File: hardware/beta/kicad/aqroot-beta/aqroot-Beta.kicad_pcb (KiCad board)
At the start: 4 copper layers, 74 x 155 mm, 187 parts, among them J1 CH280QV10-CT_50P, J2 Molex_5025700893, J3 USB_C_Receptacle_USB2.0_16P, J4 JST-PH-2 BATTERY, J5 COMMUNITY_HEADER_2x13, J6 JST-PH-2 SPEAKER, Q1 AO3400A, SW1 BOOT, SW2 UP, SW3 DOWN, SW4 LEFT, SW5 RIGHT, SW6 A_SELECT, SW7 B_BACK, SW8 HOME, SW9 SW_SPDT, U1 ESP32-S3-WROOM-1, U10 USBLC6-2SC6, U11 BQ25185, U12 TPS63020, U13 TPS61023, U14 MAX17048, U15 TPS22918, U16 TCA9517ADGK, U17 TPS61169DCKR, U2 TCA9535PWR, U3 TCA9535PWR, U4 BMI270, U5 MAX98357A, U6 TSOP38238, U7 E07-400M10S, U8 E22-900M22S, U9 ST25R3916-AQET

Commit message: AQROOT Beta: close final routing blockers
Closes the two BLOCKS_ROUTING items left by the pre-routing rule pass.
No traces drawn, no component moved, aqroot-Beta.kicad_dru untouched.

1. BQ25185 charge current locked at 300 mA.

R37 2k 1% -> 1k 1% on the ISET pin. ICHG = KISET/RISET = 300/1000 =
300 mA typ, 285/300/315 mA from the KISET spread and 270-330 mA at
TI's +/-10% ICHG_ACC spec. 0.15 C on the 2000 mAh Beta pack. IPRECHG
rises to 60 mA and ITERM to 30 mA. 1 kohm is TI's own figure in
SLUSF65A section 8.2.2.2, is far above RISET_SHORT (264 ohm), and
300 mA is far below the 1 A device maximum, so nothing is clipped.

R36 = 18 kohm is untouched: the input current limit stays ILIM500
(450/475/498 mA) and VBATREG stays 4.2 V. Both the schematic symbol and
the PCB footprint Value field were updated together, so parity picks up
no new field mismatch.

No power netclass width target changes. VBUS_CHG is set by ILIM, which
did not move; BAT_MAIN is sized by 1.5 A discharge and 3.125 A OCP;
SYS_MAIN is sized by the ~750 mA system load. IPC-2221B needs 0.057 mm
for 300 mA on 1 oz outer copper at dT=10 K, an order of magnitude below
every existing floor, so nothing was widened.

The real consequence is thermal and lands on U11. As a linear charger
with a power path, worst-case dissipation rises from ~0.46 W to ~0.69 W
(0.238 W on IN->SYS at 475 mA plus 0.450 W on the BATFET at 300 mA into
a depleted 3.0 V pack) in a 2.2 x 2.0 mm WSON-10. TREG folds charge
current back rather than failing, so this is a charge-time risk, but
U11's exposed-pad thermal vias are now required rather than optional
and the plan is revised from 1 to 2 THERMAL-class vias. Implementation
stays deferred to the routing/thermal pass.

Added BOM VERIFY: the cell/pack must permit >=300 mA charge, including
the pack protection circuit's own rating. Blocks BOM lock, not routing.

2. USB differential net names normalised to a _P/_N suffix.

  USB_D_P_CONN -> USB_D_CONN_P    USB_D_N_CONN -> USB_D_CONN_N
  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
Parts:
- R37: value 2k 1% -> 1k 1%
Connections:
- net /01_POWER_TREE/USB_D_N_CONN renamed /01_POWER_TREE/USB_D_CONN_N
- net /01_POWER_TREE/USB_D_N_ESD renamed /01_POWER_TREE/USB_D_ESD_N
- net /01_POWER_TREE/USB_D_P_CONN renamed /01_POWER_TREE/USB_D_CONN_P
- net /01_POWER_TREE/USB_D_P_ESD renamed /01_POWER_TREE/USB_D_ESD_P
- net /USB_D_N_MCU renamed /USB_D_MCU_N
- net /USB_D_P_MCU renamed /USB_D_MCU_P
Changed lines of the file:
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@@
 			(layers "F.Cu" "F.Mask" "F.Paste")
 			(roundrect_rratio 0.25)
-			(net "/01_POWER_TREE/USB_D_N_ESD")
+			(net "/01_POWER_TREE/USB_D_ESD_N")
 		)
 		(pad "2" smd roundrect
@@
 			(layers "F.Cu" "F.Mask" "F.Paste")
 			(roundrect_rratio 0.25)
-			(net "/USB_D_N_MCU")
+			(net "/USB_D_MCU_N")
 		)
 		(embedded_fonts no)
@@
 			(layers "F.Cu" "F.Mask" "F.Paste")
 			(roundrect_rratio 0.25)
-			(net "/USB_D_N_MCU")
+			(net "/USB_D_MCU_N")
 		)
 		(pad "2" smd roundrect
@@
 			(layers "F.Cu" "F.Mask" "F.Paste")
 			(roundrect_rratio 0.25)
-			(net "/USB_D_P_MCU")
+			(net "/USB_D_MCU_P")
 		)
 		(pad "2" smd roundrect
@@
 			(layers "F.Cu" "F.Mask" "F.Paste")
 			(roundrect_rratio 0.25)
-			(net "/01_POWER_TREE/USB_D_P_ESD")
+			(net "/01_POWER_TREE/USB_D_ESD_P")
 		)
 		(pad "2" smd roundrect
@@
 			(layers "F.Cu" "F.Mask" "F.Paste")
 			(roundrect_rratio 0.25)
-			(net "/USB_D_P_MCU")
+			(net "/USB_D_MCU_P")
 		)
 		(embedded_fonts no)
@@
 			)
 		)
-		(property "Value" "2k 1%"
+		(property "Value" "1k 1%"
 			(at 0 1.43 0)
 			(layer "F.Fab")
@@
 			(layers "F.Cu" "F.Mask" "F.Paste")
 			(roundrect_rratio 0.25)
-			(net "/01_POWER_TREE/USB_D_N_CONN")
+			(net "/01_POWER_TREE/USB_D_CONN_N")
 		)
 		(pad "2" smd roundrect
@@
 			(layers "F.Cu" "F.Mask" "F.Paste")
 			(roundrect_rratio 0.25)
-			(net "/01_POWER_TREE/USB_D_P_CONN")
+			(net "/01_POWER_TREE/USB_D_CONN_P")
 		)
 		(pad "4" smd roundrect
@@
 			(layers "F.Cu" "F.Mask" "F.Paste")
 			(roundrect_rratio 0.25)
-			(net "/01_POWER_TREE/USB_D_P_ESD")
+			(net "/01_POWER_TREE/USB_D_ESD_P")
 		)
 		(pad "5" smd roundrect
@@
 			(layers "F.Cu" "F.Mask" "F.Paste")
 			(roundrect_rratio 0.25)
-			(net "/01_POWER_TREE/USB_D_N_ESD")
+			(net "/01_POWER_TREE/USB_D_ESD_N")
 		)
 		(embedded_fonts no)
@@
 			(layers "F.Cu" "F.Mask" "F.Paste")
 			(roundrect_rratio 0.25)
-			(net "/01_POWER_TREE/USB_D_P_CONN")
+			(net "/01_POWER_TREE/USB_D_CONN_P")
 		)
 		(pad "A7" smd roundrect
@@
 			(layers "F.Cu" "F.Mask" "F.Paste")
 			(roundrect_rratio 0.25)
-			(net "/01_POWER_TREE/USB_D_N_CONN")
+			(net "/01_POWER_TREE/USB_D_CONN_N")
 		)
 		(pad "A8" smd roundrect
@@
 			(layers "F.Cu" "F.Mask" "F.Paste")
 			(roundrect_rratio 0.25)
-			(net "/01_POWER_TREE/USB_D_P_CONN")
+			(net "/01_POWER_TREE/USB_D_CONN_P")
 		)
 		(pad "B7" smd roundrect
@@
 			(layers "F.Cu" "F.Mask" "F.Paste")
 			(roundrect_rratio 0.25)
-			(net "/01_POWER_TREE/USB_D_N_CONN")
+			(net "/01_POWER_TREE/USB_D_CONN_N")
 		)
 		(pad "B8" smd roundrect
@@
 			(size 1.5 0.9)
 			(layers "B.Cu" "B.Mask" "B.Paste")
-			(net "/USB_D_N_MCU")
+			(net "/USB_D_MCU_N")
 		)
 		(pad "14" smd rect
@@
 			(size 1.5 0.9)
 			(layers "B.Cu" "B.Mask" "B.Paste")
-			(net "/USB_D_P_MCU")
+			(net "/USB_D_MCU_P")
 		)
 		(pad "15" smd rect

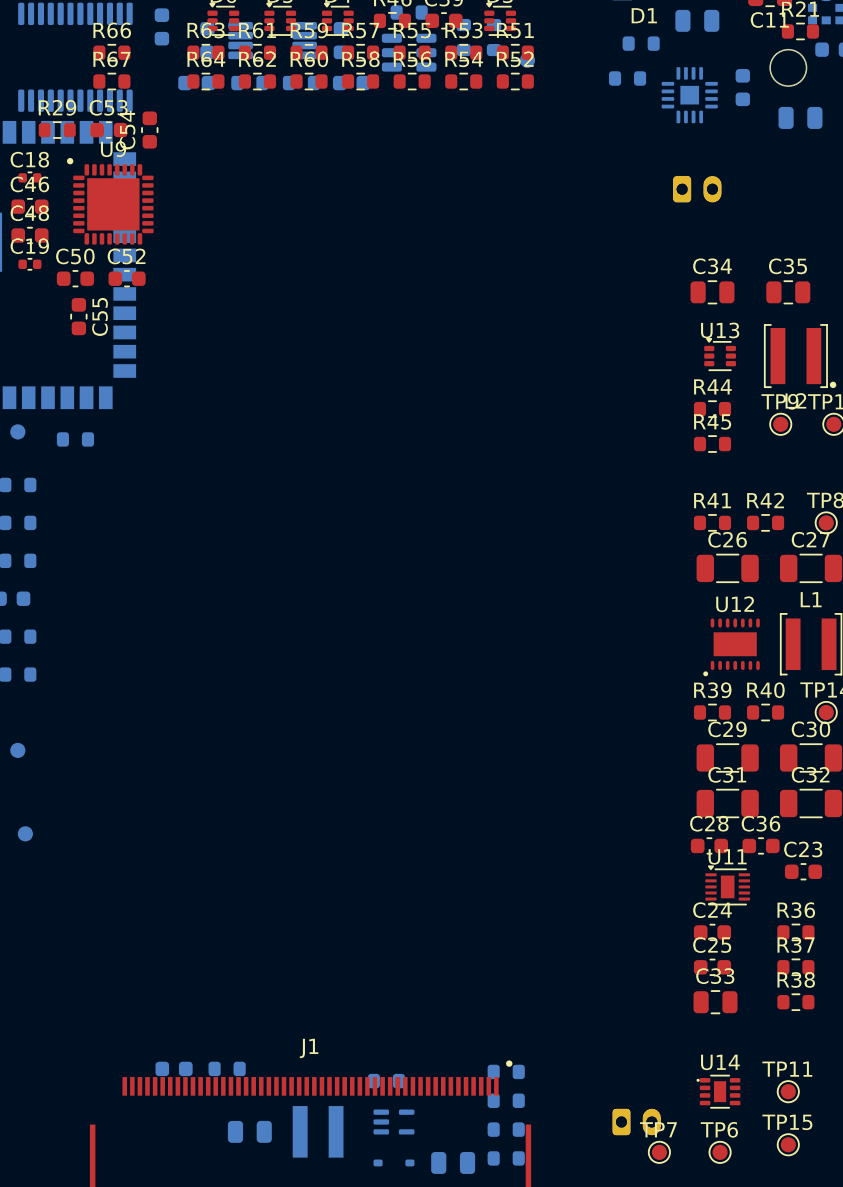
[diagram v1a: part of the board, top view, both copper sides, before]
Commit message: AQROOT Beta: route GND reference and exposed-pad thermal infrastructure
Routing Pass 1, PARTIAL. Blocks A and B of the pass scope are routed and
DRC-clean. Blocks C-F (converters, major power rails, USB, E4/E5
crossings, critical decoupling loops) were routed, produced 41 DRC
errors, and were REVERTED rather than committed. Nothing broken is in
this commit. Placement, connectivity and ERC are untouched, and no
signal trace exists on the board - GND is the only net carrying copper.

Delivered:

In1 GND reference zone, one pour inset 0.6 mm from the board edge:
10025.8 mm2 filled of an 11181.0 mm2 outline. The 1155 mm2 shortfall is
three pre-existing all-layer rule areas plus pad clearance. Two are
electrically required (WROOM antenna, NFC loop). HEADER RESERVED is a
37 x 8.5 mm hole in the reference plane with no manufacturer requirement
behind it - left in place, flagged for the CTO.

16 exposed-pad thermal vias at the THERMAL class (0.25/0.55), each array
the maximum its vendor land pattern accepts with >=0.10 mm margin. TI
SLUSF65A 8.4.1 asks for "a solid ground plane tied to the GND pin and
thermal pad" and specifies no via count, so none was invented. U11 2,
U12 6, U9 6, U5 1, U14 1. U1 needed nothing: the WROOM footprint already
carries 12 integral plated 0.20 mm vias in pad 41.

U9's exposed pad sits on top of the WROOM pad column: U1's B.Cu pads
15-30 occupy X 24.500-26.000 directly beneath the eastern half of U9's
EP land, so a through via there would short the NFC reader's ground to a
WROOM GPIO. Only the western strip is usable - 6 vias instead of 9, all
offset to one side. Placement-stack consequence, carried as an RF and
thermal review item.

KiCad custom-rule precedence is LAST-match-wins, established empirically
twice in this pass because the first assumption was wrong. aqroot-Beta
.kicad_dru now ends with an explicit PRECEDENCE TAIL documenting the
required weakest-first order: RF and rail rules, then pad-escape
necking, then land-pattern rules. Movin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
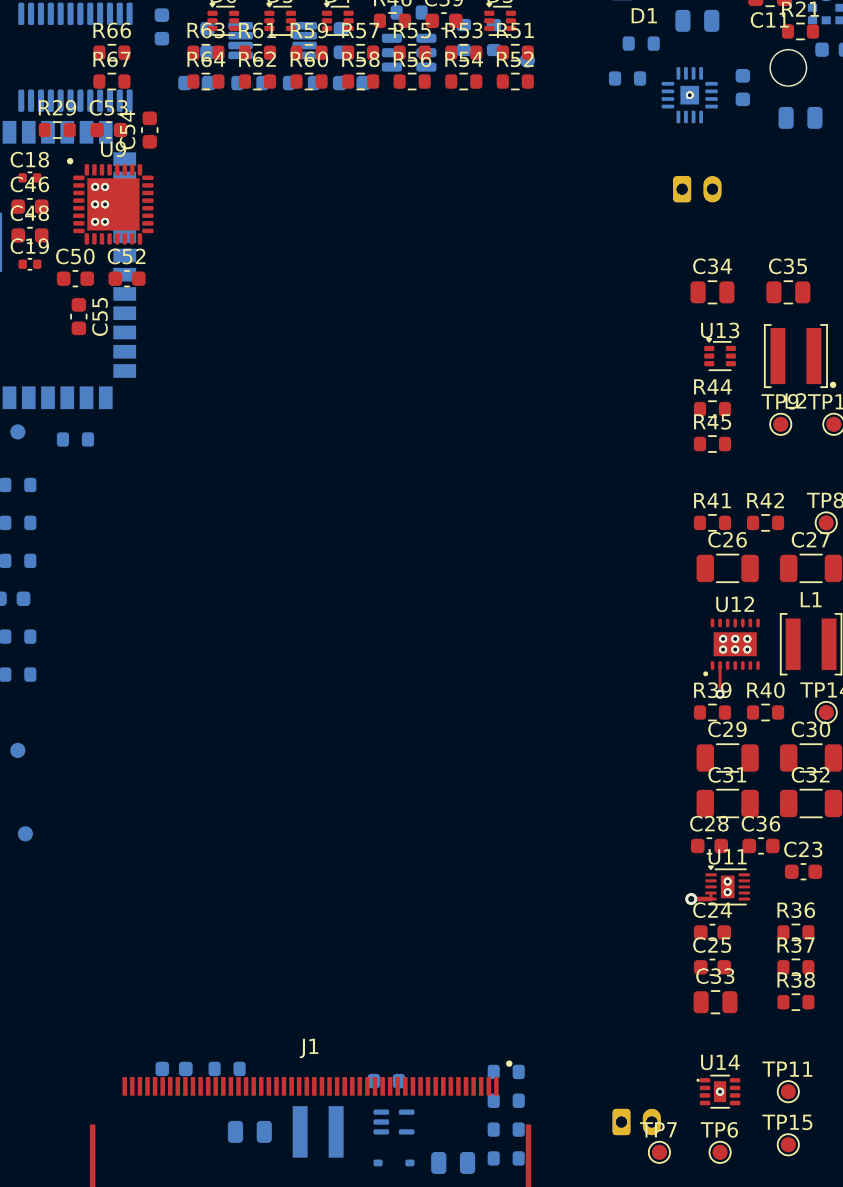
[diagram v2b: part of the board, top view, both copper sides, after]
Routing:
- net GND: track 0.00 -> 3.20 mm, vias 0 -> 18
- added copper zone on In1.Cu, net GND
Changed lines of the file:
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@@
 	(footprint "C_0603_1608Metric"
 		(layer "F.Cu")
-		(at 22 26.9)
+		(at 22.225 29.4 -90)
 		(descr "Capacitor SMD 0603 (1608 Metric), square (rectangular) end terminal, IPC-7351 nominal, (Body size source: IPC-SM-782 page 76, https://www.pcb-3d.com/wordpress/wp-content/uploads/ipc-sm-782a_amendment_1_and_2.pdf)")
 		(tags "capacitor")
-		(property "Reference" "C50"
-			(at 0 -1.43 0)
+		(property "Reference" "C55"
+			(at 0 -1.43 270)
 			(layer "F.SilkS")
 			(effects
@@
 			)
 		)
-		(property "Value" "10nF"
-			(at 0 1.43 0)
+		(property "Value" "2.2uF"
+			(at 0 1.43 270)
 			(layer "F.Fab")
 			(effects
@@
 		)
 		(property "Datasheet" ""
-			(at 0 0 0)
+			(at 0 0 270)
 			(layer "F.Fab")
 			(hide yes)
@@
 		)
 		(property "Description" ""
-			(at 0 0 0)
+			(at 0 0 270)
 			(layer "F.Fab")
 			(hide yes)
@@
 		)
 		(property "KiLib_Generator" "SMD_2terminal_chip_molded"
-			(at 0 0 0)
+			(at 0 0 270)
 			(layer "F.SilkS")
 			(hide yes)
@@
 		(duplicate_pad_numbers_are_jumpers no)
 		(fp_line
-			(start -0.14058 -0.51)
-			(end 0.14058 -0.51)
+			(start -0.14058 0.51)
+			(end 0.14058 0.51)
 			(stroke
 				(width 0.12)
@@
 		)
 		(fp_line
-			(start -0.14058 0.51)
-			(end 0.14058 0.51)
+			(start -0.14058 -0.51)
+			(end 0.14058 -0.51)
 			(stroke
 				(width 0.12)
@@
 		)
 		(fp_text user "${REFERENCE}"
-			(at 0 0 0)
+			(at 0 0 270)
 			(layer "F.Fab")
 			(effects
@@
 		)
 		(pad "1" smd roundrect
-			(at -0.775 0)
+			(at -0.775 0 270)
 			(size 0.9 0.95)
 			(layers "F.Cu" "F.Mask" "F.Paste")
 			(roundrect_rratio 0.25)
-			(net "/04_SPI_B_RADIOS_NFC/NFC_VDD_RF")
+			(net "/NFC_5V_PA_PENDING")
 		)
 		(pad "2" smd roundrect
-			(at 0.775 0)
+			(at 0.775 0 270)
 			(size 0.9 0.95)
 			(layers "F.Cu" "F.Mask" "F.Paste")
@@
 	(footprint "C_0603_1608Metric"
 		(layer "F.Cu")
-		(at 22.225 29.4 -90)
+		(at 22 26.9)
 		(descr "Capacitor SMD 0603 (1608 Metric), square (rectangular) end terminal, IPC-7351 nominal, (Body size source: IPC-SM-782 page 76, https://www.pcb-3d.com/wordpress/wp-content/uploads/ipc-sm-782a_amendment_1_and_2.pdf)")
 		(tags "capacitor")
-		(property "Reference" "C55"
-			(at 0 -1.43 270)
+		(property "Reference" "C50"
+			(at 0 -1.43 0)
 			(layer "F.SilkS")
 			(effects
@@
 			)
 		)
-		(property "Value" "2.2uF"
-			(at 0 1.43 270)
+		(property "Value" "10nF"
+			(at 0 1.43 0)
 			(layer "F.Fab")
 			(effects
@@
 		)
 		(property "Datasheet" ""
-			(at 0 0 270)
+			(at 0 0 0)
 			(layer "F.Fab")
 			(hide yes)
@@
 		)
 		(property "Description" ""
-			(at 0 0 270)
+			(at 0 0 0)
 			(layer "F.Fab")
 			(hide yes)
@@
 		)
 		(property "KiLib_Generator" "SMD_2terminal_chip_molded"
-			(at 0 0 270)
+			(at 0 0 0)
 			(layer "F.SilkS")
 			(hide yes)
@@
 		(duplicate_pad_numbers_are_jumpers no)
 		(fp_line
-			(start -0.14058 0.51)
-			(end 0.14058 0.51)
+			(start -0.14058 -0.51)
+			(end 0.14058 -0.51)
 			(stroke
 				(width 0.12)
@@
 		)
 		(fp_line
-			(start -0.14058 -0.51)
-			(end 0.14058 -0.51)
+			(start -0.14058 0.51)
+			(end 0.14058 0.51)
 			(stroke
 				(width 0.12)
@@
 		)
 		(fp_text user "${REFERENCE}"
-			(at 0 0 270)
+			(at 0 0 0)
 			(layer "F.Fab")
 			(effects
@@
 		)
 		(pad "1" smd roundrect
-			(at -0.775 0 270)
+			(at -0.775 0)
 			(size 0.9 0.95)
 			(layers "F.Cu" "F.Mask" "F.Paste")
 			(roundrect_rratio 0.25)
-			(net "/NFC_5V_PA_PENDING")
+			(net "/04_SPI_B_RADIOS_NFC/NFC_VDD_RF")
 		)
 		(pad "2" smd roundrect
-			(at 0.775 0 270)
+			(at 0.775 0)
 			(size 0.9 0.95)
 			(layers "F.Cu" "F.Mask" "F.Paste")
@@
 		)
 	)
+	(segment
+		(start 63.9 67.4)
+		(end 63.9 67.8)
+		(width 0.2)
+		(layer "F.Cu")
+		(net "GND")
+	)
+	(segment
+		(start 64.5 52.4)
+		(end 64.5 53.9)
+		(width 0.2)
+		(layer "F.Cu")
+		(net "GND")
+	)
+	(segment
+		(start 63.9 67.8)
+		(end 62.6 67.8)
+		(width 0.3)
+		(layer "F.Cu")
+		(net "GND")
+	)
+	(via
+		(at 62.5 14.8)
+		(size 0.55)
+		(drill 0.25)
+		(layers "F.Cu" "B.Cu")
+		(net "GND")
+	)
+	(via
+		(at 23.3 22)
+		(size 0.55)
+		(drill 0.25)
+		(layers "F.Cu" "B.Cu")
+		(net "GND")
+	)
+	(via
+		(at 62.6 67.8)
+		(size 0.8)
+		(drill 0.4)
+		(layers "F.Cu" "B.Cu")
+		(net "GND")
+	)
+	(via
+		(at 65 66.65)
+		(size 0.55)
+		(drill 0.25)
+		(layers "F.Cu" "B.Cu")
+		(net "GND")
+	)
+	(via
+		(at 64.5 80.5)
+		(size 0.55)
+		(drill 0.25)
+		(layers "F.Cu" "B.Cu")
+		(net "GND")
+	)
+	(via
+		(at 64.5 54.3)
+		(size 0.6)
+		(drill 0.3)
+		(layers "F.Cu" "B.Cu")
+		(net "GND")
+	)
+	(via
+		(at 23.3 20.85)
+		(size 0.55)
+		(drill 0.25)
+		(layers "F.Cu" "B.Cu")
+		(net "GND")
+	)
+	(via
+		(at 66.3 50.65)
+		(size 0.55)
+		(drill 0.25)
+		(layers "F.Cu" "B.Cu")
+		(net "GND")
+	)
+	(via
+		(at 65.5 51.35)
+		(size 0.55)
+		(drill 0.25)
+		(layers "F.Cu" "B.Cu")
+		(net "GND")
+	)
+	(via
+		(at 23.3 23.15)
+		(size 0.55)
+		(drill 0.25)
+		(layers "F.Cu" "B.Cu")
+		(net "GND")
+	)
+	(via
+		(at 65.5 50.65)
+		(size 0.55)
+		(drill 0.25)
+		(layers "F.Cu" "B.Cu")
+		(net "GND")
+	)
+	(via
+		(at 23.95 20.85)
+		(size 0.55)
+		(drill 0.25)
+		(layers "F.Cu" "B.Cu")
+		(net "GND")
+	)
+	(via
+		(at 65 67.35)
+		(size 0.55)
+		(drill 0.25)
+		(layers "F.Cu" "B.Cu")
+		(net "GND")
+	)
+	(via
+		(at 66.3 51.35)
+		(size 0.55)
+		(drill 0.25)
+		(layers "F.Cu" "B.Cu")
+		(net "GND")
+	)
+	(via
+		(at 64.7 51.35)
+		(size 0.55)
+		(drill 0.25)
+		(layers "F.Cu" "B.Cu")
+		(net "GND")
+	)
+	(via
+		(at 23.95 22)
+		(size 0.55)
+		(drill 0.25)
+		(layers "F.Cu" "B.Cu")
+		(net "GND")
+	)
+	(via
+		(at 64.7 50.65)
+		(size 0.55)
+		(drill 0.25)
+		(layers "F.Cu" "B.Cu")
+		(net "GND")
+	)
+	(via
+		(at 23.95 23.15)
+		(size 0.55)
+		(drill 0.25)
+		(layers "F.Cu" "B.Cu")
+		(net "GND")
+	)
 	(zone
 		(layers "F.Cu" "B.Cu" "In1.Cu" "In2.Cu")
@@
 			)
 		)
+	)
+	(zone
+		(net "GND")
+		(layer "In1.Cu")
+		(name "In1 GND REFERENCE")
+		(hatch edge 0.5)
+		(connect_pads yes
+			(clearance 0.25)
+		)
+		(min_thickness 0.25)
+		(fill yes
+			(thermal_gap 0.5)
+			(thermal_bridge_width 0.5)
+			(island_removal_mode 0)
+		)
+		(polygon
+			(pts
+				(xy 0.6 3.4) (xy 3.4 0.6) (xy 70.6 0.6) (xy 73.4 3.4) (xy 73.4 151.6) (xy 70.6 154.4) (xy 3.4 154.4)
+				(xy 0.6 151.6)
+			)
+		)
